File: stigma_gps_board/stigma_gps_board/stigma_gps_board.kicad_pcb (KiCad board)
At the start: 2 copper layers, 0 parts

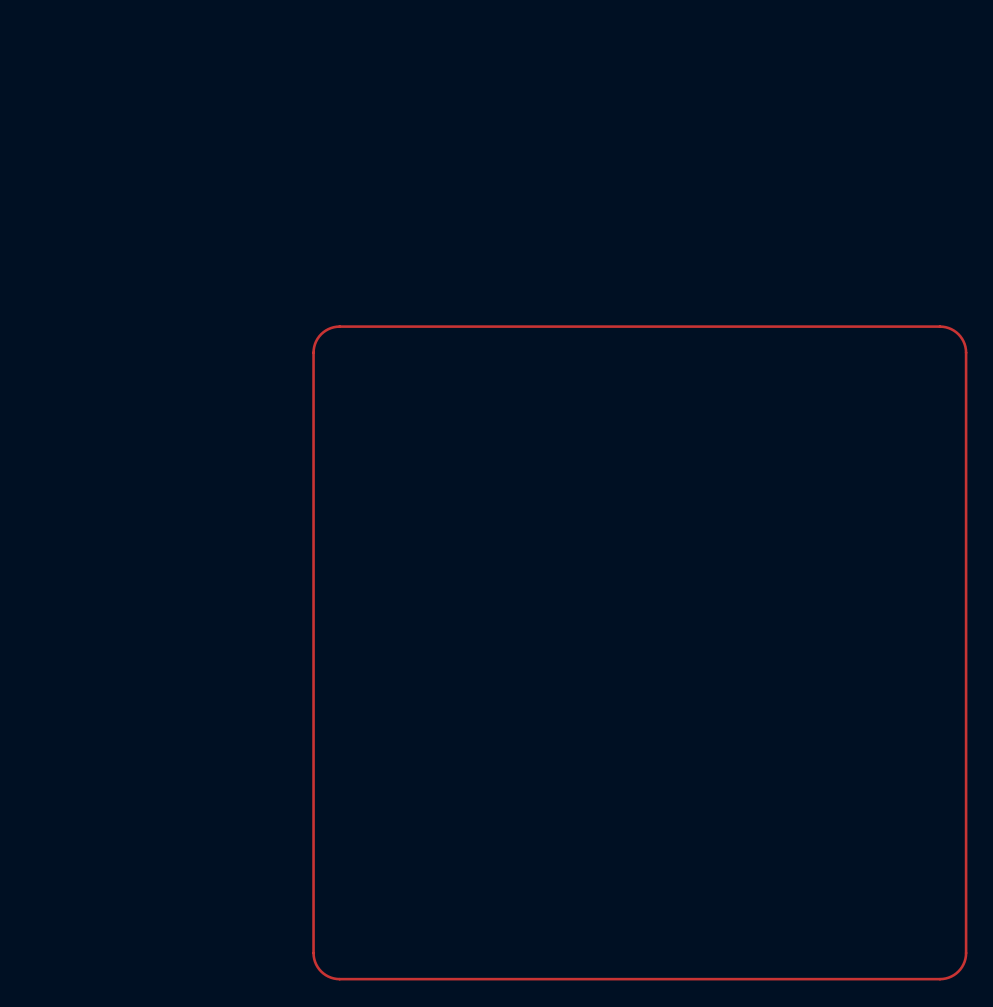
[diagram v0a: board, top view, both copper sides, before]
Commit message: first revision of gps board finished
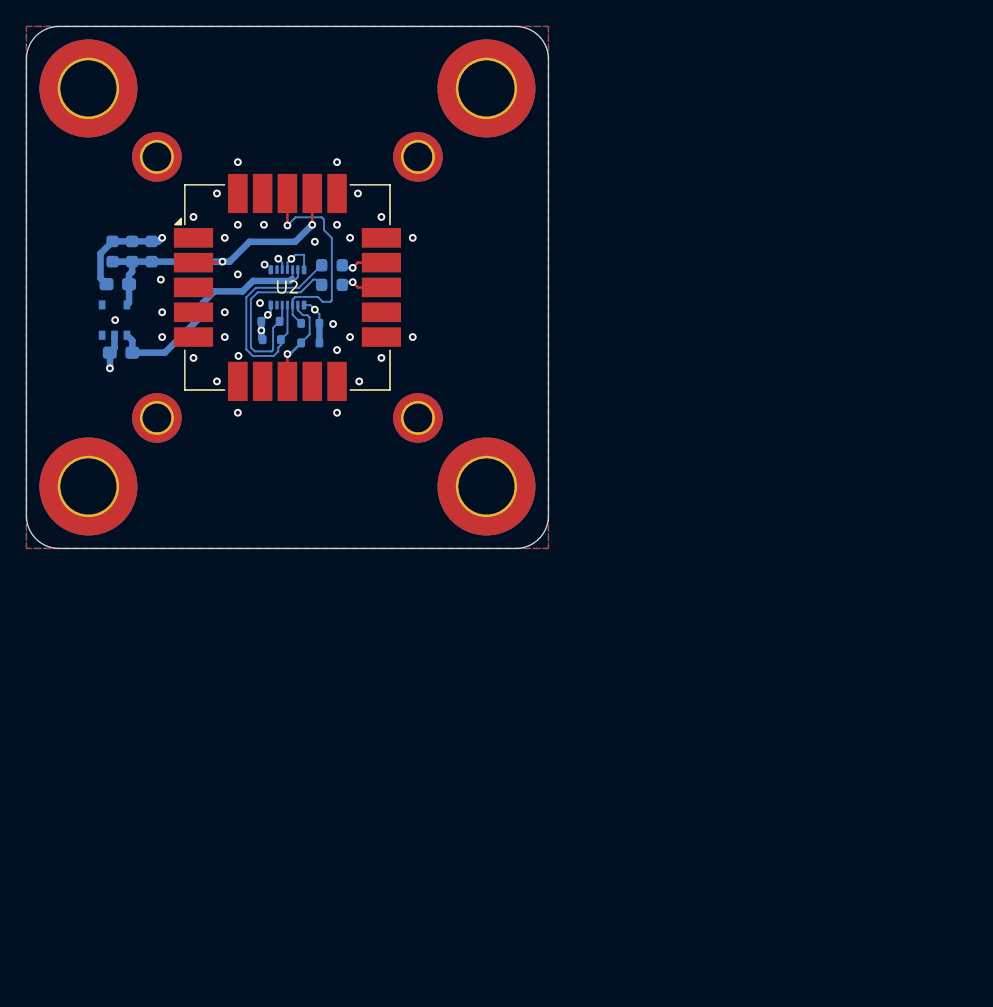
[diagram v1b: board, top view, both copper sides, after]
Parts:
- added C1: 1uF, Capacitor_SMD:C_0603_1608Metric_Pad1.08x0.95mm_HandSolder, B.Cu at (107.2, 75.0)
- added C2: 1uF, Capacitor_SMD:C_0603_1608Metric_Pad1.08x0.95mm_HandSolder, B.Cu at (107.0, 69.8)
- added C3: 100n, Capacitor_SMD:C_0603_1608Metric, B.Cu at (109.6, 67.2)
- added C4: 100n, Capacitor_SMD:C_0603_1608Metric, B.Cu at (108.1, 67.2)
- added C5: 100n, Capacitor_SMD:C_0603_1608Metric, B.Cu at (106.6, 67.2)
- added D1: ESD5Zxx, Diode_SMD:D_SOD-523, B.Cu at (121.8, 72.8)
- added D2: ESD5Zxx, Diode_SMD:D_SOD-523, B.Cu at (121.8, 74.2)
- added D3: ESD5Zxx, Diode_SMD:D_SOD-523, B.Cu at (118.7, 72.6)
- added D4: ESD5Zxx, Diode_SMD:D_SOD-523, B.Cu at (118.8, 74.0)
- added H1: MountingHole_Pad, MountingHole:MountingHole_2.2mm_M2_DIN965_Pad_TopBottom, F.Cu at (110.0, 60.0)
- added H2: MountingHole_Pad, MountingHole:MountingHole_2.2mm_M2_DIN965_Pad_TopBottom, F.Cu at (130.0, 80.0)
- added H3: MountingHole_Pad, MountingHole:MountingHole_2.2mm_M2_DIN965_Pad_TopBottom, F.Cu at (130.0, 60.0)
- added H4: MountingHole_Pad, MountingHole:MountingHole_2.2mm_M2_DIN965_Pad_TopBottom, F.Cu at (110.0, 80.0)
- added H5: MountingHole_Pad, MountingHole:MountingHole_4.3mm_M4_DIN965_Pad_TopBottom, F.Cu at (104.8, 54.8)
- added H6: MountingHole_Pad, MountingHole:MountingHole_4.3mm_M4_DIN965_Pad_TopBottom, F.Cu at (135.2, 54.8)
- added H7: MountingHole_Pad, MountingHole:MountingHole_4.3mm_M4_DIN965_Pad_TopBottom, F.Cu at (104.8, 85.2)
- added H8: MountingHole_Pad, MountingHole:MountingHole_4.3mm_M4_DIN965_Pad_TopBottom, F.Cu at (135.2, 85.2)
- added J1: Conn_02x05_Top_Bottom, stigma:DF40GB-10DP-0.4V-plug, B.Cu at (120.0, 70.0)
- added L1: BEAD, Inductor_SMD:L_0603_1608Metric, B.Cu at (123.4, 68.3)
- added L2: BEAD, Inductor_SMD:L_0603_1608Metric, B.Cu at (123.4, 69.8)
- added U1: NCP115AMX120TCG, Package_SO:TSOP-5_1.65x3.05mm_P0.95mm, B.Cu at (106.8, 72.5)
- added U2: SAM-M10Q, RF_GPS:ublox_SAM-M8Q_HandSolder, F.Cu at (120.0, 70.0)
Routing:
- net +3.3V: track 0.00 -> 24.6 mm, vias 0 -> 2
- net GND: track 0.00 -> 21.4 mm, vias 0 -> 40
- net 5V: track 0.00 -> 18.4 mm
- net UART2_TX: track 0.00 -> 17.8 mm
- net GPS_RESET: track 0.00 -> 17.4 mm, vias 0 -> 1
- net UART2_RX: track 0.00 -> 15.7 mm
- net GPS_SAFEBOOT: track 0.00 -> 7.24 mm, vias 0 -> 1
- net Net-(U2-TXD): track 0.00 -> 3.25 mm, vias 0 -> 1
- net Net-(U2-RXD): track 0.00 -> 3.25 mm, vias 0 -> 1
- added copper zone on B.Cu, net GND
- added copper zone on F.Cu, net GND
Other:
- board outline added: 40 x 40 mm
